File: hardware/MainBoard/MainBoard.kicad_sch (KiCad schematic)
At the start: 5 parts, among them J1 Conn_01x08_Socket, J2 Conn_01x08_Socket, J3 Conn_01x08_Socket, J4 Micro_SD_Card_Det2, U1 ESP32-S3-WROOM-1

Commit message: added more stuff to main board
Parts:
- added BZ1: Buzzer, Buzzer_Beeper:Buzzer_Mallory_AST1109MLTRQ, symbol Device:Buzzer
- added P1: USB_C_Plug_USB2.0, Connector_USB:USB_C_Receptacle_Amphenol_12401610E4-2A, symbol Connector:USB_C_Plug_USB2.0
- J4: footprint (none) -> Connector_Card:microSD_HC_Hirose_DM3AT-SF-PEJM5
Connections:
- net USB-: now reaches U1.13 (USB_D-)
- net USB-: now also P1.A7 (D-)
- net USB+: now reaches U1.14 (USB_D+)
- net USB+: now also P1.A6 (D+)
- new net: P1.A1 (GND), P1.A12 (GND), P1.B1 (GND), P1.B12 (GND)
- new net: P1.A4 (VBUS), P1.A9 (VBUS), P1.B4 (VBUS), P1.B9 (VBUS)
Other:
- moved on the sheet: J1, J3, U1

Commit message: finished usb and voltage regulator
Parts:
- removed P1: USB_C_Plug_USB2.0, Connector_USB:USB_C_Receptacle_Amphenol_12401610E4-2A, symbol Connector:USB_C_Plug_USB2.0
- added C1: 10uF, symbol Device:C
- added C2, C4: 10uF, symbol Device:C_Small
- added C3, C5: 0u1F, symbol Device:C_Small
- added D1: 1N5819WS, Diode_SMD:D_SOD-323, symbol Diode:1N5819WS
- added D2, D3, D4: D_TVS_Small_Filled, symbol Device:D_TVS_Small_Filled
- added D5: PWRLED, symbol Device:LED
- added J5: USB_C_Receptacle_USB2.0_16P, symbol Connector:USB_C_Receptacle_USB2.0_16P
- added R1, R2: 5k1, symbol Device:R
- added R3: 75, symbol Device:R_Small
- added U2: AMS1117-3.3, Package_TO_SOT_SMD:SOT-223-3_TabPin2, symbol Regulator_Linear:AMS1117-3.3
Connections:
- net GND: now also C1.2, C2.2, C3.2, C4.2, C5.2, D2.2 (A2), D3.2 (A2), D4.2 (A2), D5.1 (K), J5.A1 (GND), J5.A12 (GND), J5.B1 (GND), J5.B12 (GND), J5.S1 (SHIELD), R1.2, R2.2, U2.1 (GND)
- net USB+: now also D4.1 (A1), J5.A6 (D+), J5.B6 (D+)
- net USB-: now also D3.1 (A1), J5.A7 (D-), J5.B7 (D-)
- new net: J5.A5 (CC1), R2.1
- new net: D1.2 (A), D2.1 (A1), J5.A4 (VBUS), J5.A9 (VBUS), J5.B4 (VBUS), J5.B9 (VBUS)
- new net: J5.B5 (CC2), R1.1
- new net: D5.2 (A), R3.2
- new net VCC_3V3: C4.1, C5.1, R3.1, U2.2 (VO)
- new net VCC_5V: C1.1, C2.1, C3.1, D1.1 (K), U2.3 (VI)
- no-connect marks 0 -> 2
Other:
- note added: "USB-C"
- note added: "Voltage Regulator"
- moved on the sheet: J1, J2, J3

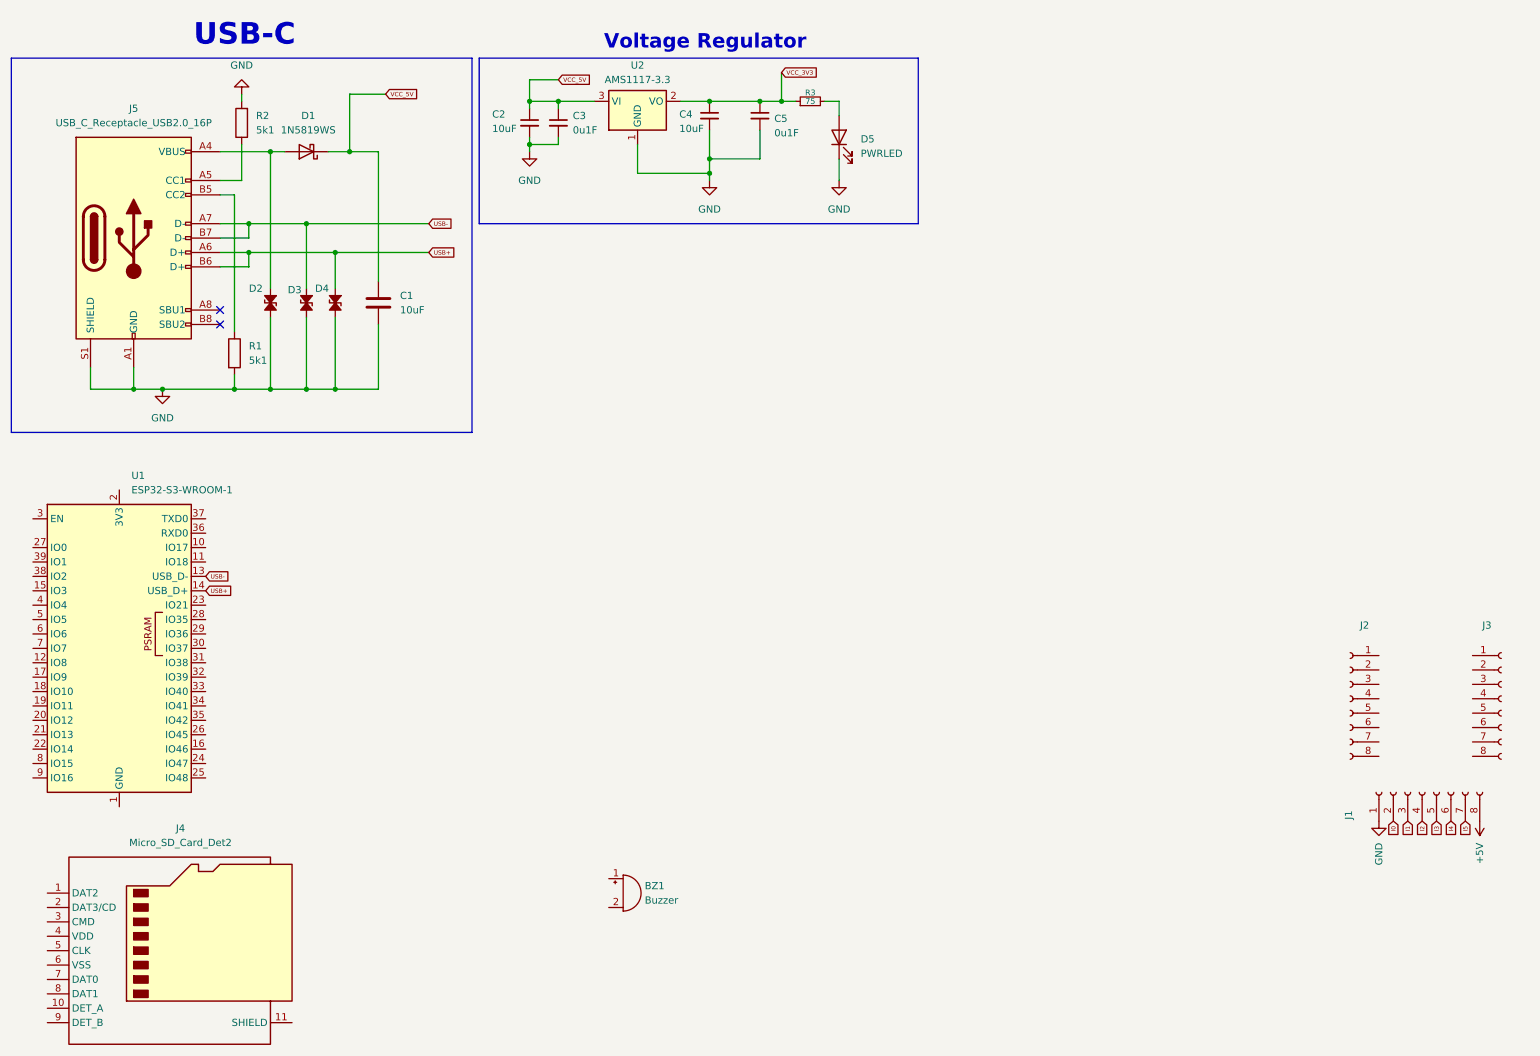
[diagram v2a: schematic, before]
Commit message: added buttons to main board
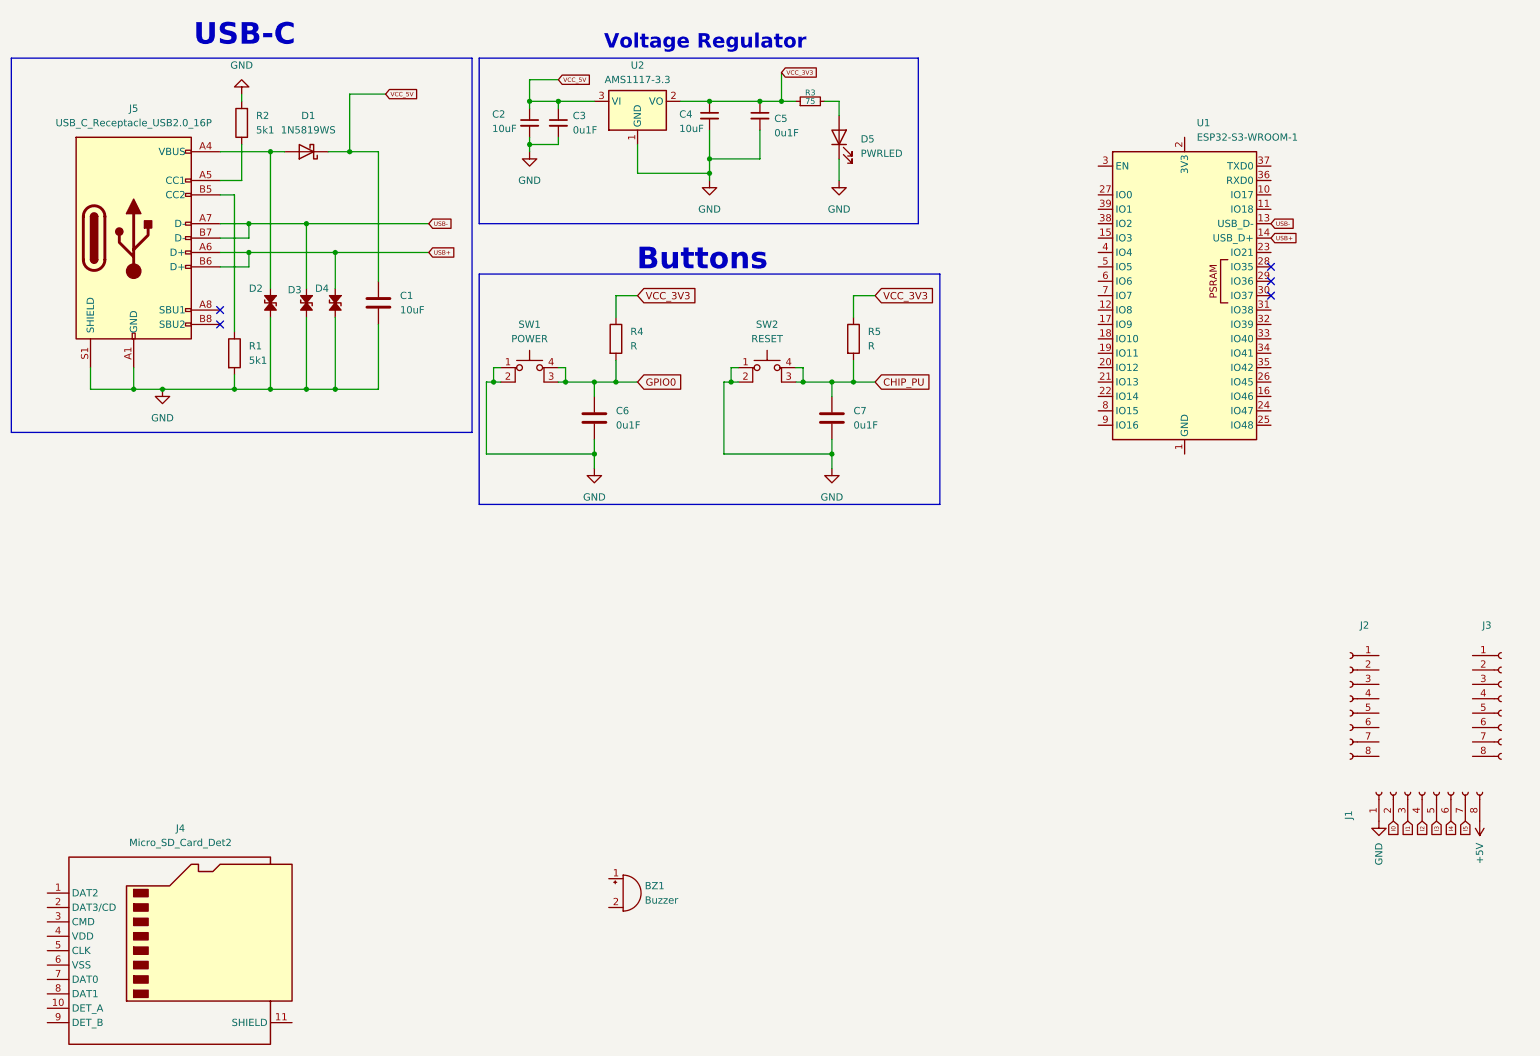
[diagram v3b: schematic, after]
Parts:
- added C6, C7: 0u1F, symbol Device:C
- added R4, R5: R, symbol Device:R
- added SW1: POWER, symbol Switch:SW_MEC_5E
- added SW2: RESET, symbol Switch:SW_MEC_5E
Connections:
- net GND: now also C6.2, C7.2, SW1.1, SW1.2, SW2.1, SW2.2
- net VCC_3V3: now also R4.1, R5.1
- new net CHIP_PU: C7.1, R5.2, SW2.3 (K), SW2.4 (A)
- new net GPIO0: C6.1, R4.2, SW1.3 (K), SW1.4 (A)
- no-connect marks 2 -> 5
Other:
- note added: "Buttons"
- moved on the sheet: U1

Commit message: added another voltage regulator
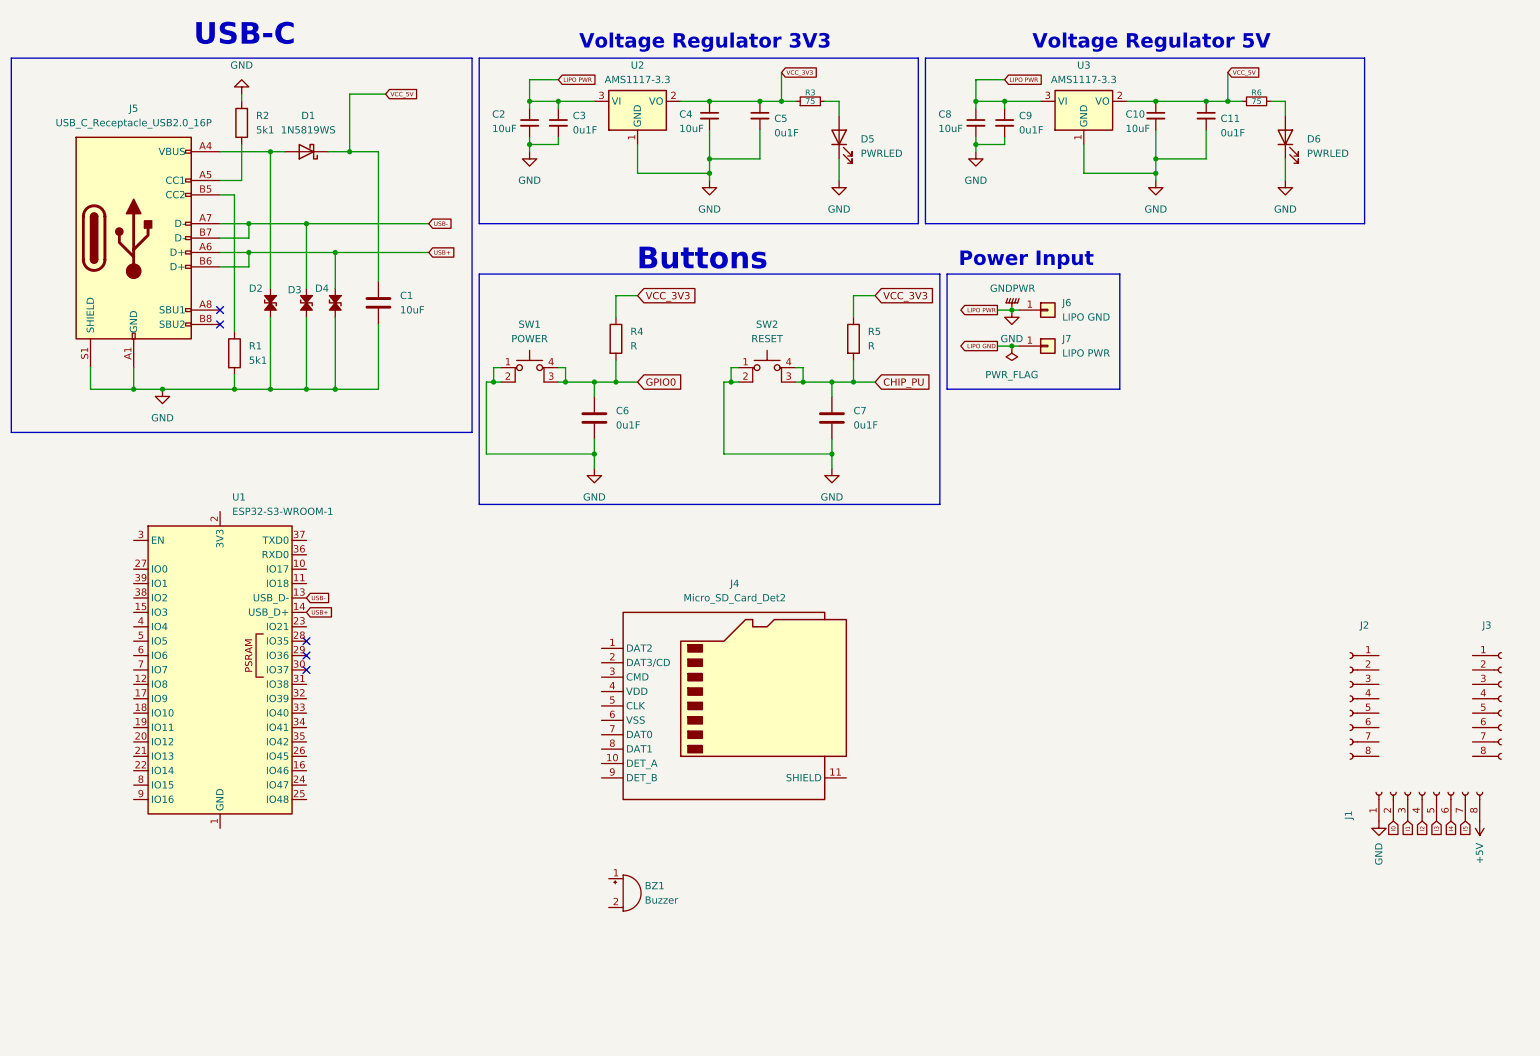
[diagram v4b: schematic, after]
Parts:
- added C10, C8: 10uF, symbol Device:C_Small
- added C11, C9: 0u1F, symbol Device:C_Small
- added D6: PWRLED, symbol Device:LED
- added J6: LIPO GND, TestPoint:TestPoint_Pad_4.0x4.0mm, symbol Connector_Generic:Conn_01x01
- added J7: LIPO PWR, TestPoint:TestPoint_Pad_4.0x4.0mm, symbol Connector_Generic:Conn_01x01
- added R6: 75, symbol Device:R_Small
- added U3: AMS1117-3.3, Package_TO_SOT_SMD:SOT-223-3_TabPin2, symbol Regulator_Linear:AMS1117-3.3
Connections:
- net GND: now also C2.1, C3.1, U2.3 (VI), C10.2, C11.2, C8.1, C8.2, C9.1, C9.2, D6.1 (K), J6.1 (Pin_1), U3.1 (GND), U3.3 (VI)
- net VCC_5V: now also C10.1, C11.1, R6.1, U3.2 (VO); no longer C2.1, C3.1, U2.3 (VI)
- new net: D6.2 (A), R6.2
- new net LIPO GND: J7.1 (Pin_1)
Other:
- note added: "Power Input"
- note added: "Voltage Regulator 3V3"
- note added: "Voltage Regulator 5V"
- note removed: "Voltage Regulator"
- moved on the sheet: J4, U1

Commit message: added lots of things to main board
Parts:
- removed D6: PWRLED, symbol Device:LED
- removed SW1: POWER, symbol Switch:SW_MEC_5E
- removed SW2: RESET, symbol Switch:SW_MEC_5E
- added BOOT1: RESET, Button_Switch_SMD:SW_Push_1P1T_NO_CK_KMR2, symbol Switch:SW_Push
- added C12, C15: 10uF, Capacitor_SMD:C_0805_2012Metric, symbol Device:C
- added C13: 100nF, Capacitor_SMD:C_0402_1005Metric, symbol Device:C
- added C14: 1uF, Capacitor_SMD:C_0603_1608Metric, symbol Device:C
- added C16: 0u1F, Capacitor_SMD:C_0402_1005Metric, symbol Device:C
- added R10, R12, R13, R8, R9: 10k, symbol Device:R_Small
- added R7: 10k, Resistor_SMD:R_1206_3216Metric, symbol Device:R
- added RESET1: BOOT, Button_Switch_SMD:SW_Push_1P1T_NO_CK_KMR2, symbol Switch:SW_Push
- C1, C10, C2, C4, C8: footprint (none) -> Capacitor_SMD:C_0805_2012Metric
- C11, C3, C5, C6, C7, C9: footprint (none) -> Capacitor_SMD:C_0402_1005Metric
- D2, D3, D4: footprint (none) -> Diode_SMD:D_0805_2012Metric
- D5: footprint (none) -> LED_SMD:LED_0603_1608Metric
- J5: footprint (none) -> Connector_USB:USB_C_Receptacle_GCT_USB4085
- R1, R2, R3, R6: footprint (none) -> Resistor_SMD:R_1206_3216Metric
- R4, R5: value R -> 10k; footprint (none) -> Resistor_SMD:R_1206_3216Metric
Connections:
- net I5 is gone; now on net SELECT RETURN: J1.7 (Pin_7)
- net VCC_3V3 is gone; now on net ESP_3V3: C4.1, C5.1, R3.1, R4.1, R5.1, U2.2 (VO)
- net CHIP_PU: now also U1.3 (EN), C14.1, R7.2, RESET1.2
- net GND: now also BZ1.2 (-), J4.11 (SHIELD), J4.6 (VSS), R6.2, U1.1 (GND), U1.40 (GND), U1.41 (GND), BOOT1.1, C12.2, C13.2, C14.2, C15.2, C16.2, RESET1.1; no longer C2.1, C3.1, C8.1, C9.1, J6.1 (Pin_1), U2.3 (VI), U3.3 (VI)
- net GPIO0: now also U1.27 (IO0), BOOT1.2
- net I0: now also U1.26 (IO45)
- net I1: now also U1.25 (IO48)
- net I2: now also U1.23 (IO21)
- net I3: now also U1.24 (IO47)
- net I4: now also U1.22 (IO14)
- net SD_DAT2: now reaches J4.1 (DAT2)
- net SD_DAT2: now also U1.34 (IO41), R8.2
- net SD_DET: now reaches J4.10 (DET_A)
- net SD_DET: now also J4.9 (DET_B), U1.31 (IO38)
- net SD_DAT3: now reaches J4.2 (DAT3/CD)
- net SD_DAT3: now also U1.33 (IO40), R9.2
- net SD_CMD: now reaches J4.3 (CMD)
- net SD_CMD: now also U1.32 (IO39), R10.2
- net ESP_3V3: now reaches J4.4 (VDD)
- net ESP_3V3: now also U1.2 (3V3), C12.1, C13.1, C15.1, C16.1, R10.1, R12.1, R13.1, R7.1, R8.1, R9.1
- net SD_CLK: now reaches J4.5 (CLK)
- net SD_CLK: now also U1.30 (IO37)
- net SD_DAT0: now reaches J4.7 (DAT0)
- net SD_DAT0: now also U1.29 (IO36), R12.2
- net SD_DAT1: now reaches J4.8 (DAT1)
- net SD_DAT1: now also U1.28 (IO35), R13.2
- net BZR: now reaches BZ1.1 (+)
- net SELECT RETURN: now reaches U1.21 (IO13)
- net LIPO GND renamed GNDPWR
- new net LIPO PWR: C2.1, C3.1, C8.1, C9.1, J6.1 (Pin_1), U2.3 (VI), U3.3 (VI)
- no-connect marks 5 -> 2
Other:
- note added: "Buzzer"
- note added: "ESP32-S3-WROOM-1"
- note added: "SD Card"
- moved on the sheet: BZ1, J1, J2, J3, J4, J6, J7, U1

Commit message: more main board stuff
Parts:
- BZ1: footprint Buzzer_Beeper:Buzzer_Mallory_AST1109MLTRQ -> Buzzer_Beeper:MagneticBuzzer_Kingstate_KCG0601
- R10, R12, R13, R8, R9: footprint (none) -> Resistor_SMD:R_1206_3216Metric
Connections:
- net DATA8: now reaches J2.1 (Pin_1)
- net DATA8: now also U1.7 (IO7)
- net DATA9: now reaches J2.2 (Pin_2)
- net DATA9: now also U1.8 (IO15)
- net DATA10: now reaches J2.3 (Pin_3)
- net DATA10: now also U1.9 (IO16)
- net DATA11: now reaches J2.4 (Pin_4)
- net DATA11: now also U1.10 (IO17)
- net DATA12: now reaches J2.5 (Pin_5)
- net DATA12: now also U1.11 (IO18)
- net DATA13: now reaches J2.6 (Pin_6)
- net DATA13: now also U1.12 (IO8)
- net DATA14: now reaches J2.7 (Pin_7)
- net DATA14: now also U1.15 (IO3)
- net DATA15: now reaches J2.8 (Pin_8)
- net DATA15: now also U1.16 (IO46)
- net DATA7: now reaches J3.1 (Pin_1)
- net DATA7: now also U1.35 (IO42)
- net DATA6: now reaches J3.2 (Pin_2)
- net DATA6: now also U1.36 (RXD0)
- net DATA5: now reaches J3.3 (Pin_3)
- net DATA5: now also U1.37 (TXD0)
- net DATA4: now reaches J3.4 (Pin_4)
- net DATA4: now also U1.38 (IO2)
- net DATA3: now reaches J3.5 (Pin_5)
- net DATA3: now also U1.39 (IO1)
- net DATA2: now reaches J3.6 (Pin_6)
- net DATA2: now also U1.6 (IO6)
- net DATA1: now reaches J3.7 (Pin_7)
- net DATA1: now also U1.5 (IO5)
- net DATA0: now reaches J3.8 (Pin_8)
- net DATA0: now also U1.4 (IO4)
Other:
- note added: "Hat Connection Interface"
- note added: "LiPo Power Input"
- note removed: "Power Input"
- moved on the sheet: BZ1, J1, J2, J3, J6, J7

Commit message: finished main board
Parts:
- removed RESET1: BOOT, Button_Switch_SMD:SW_Push_1P1T_NO_CK_KMR2, symbol Switch:SW_Push
- removed U3: AMS1117-3.3, Package_TO_SOT_SMD:SOT-223-3_TabPin2, symbol Regulator_Linear:AMS1117-3.3
- added D6: PWRLED, LED_SMD:LED_0603_1608Metric, symbol Device:LED
- added J8: En_A, TestPoint:TestPoint_Pad_1.5x1.5mm, symbol Connector_Generic:Conn_01x01
- added J9: En_B, TestPoint:TestPoint_Pad_1.5x1.5mm, symbol Connector_Generic:Conn_01x01
- added Q1: MMBT2222A, Package_TO_SOT_SMD:SOT-23W_Handsoldering, symbol Transistor_BJT:MMBT2222A
- added U3: AMS1117-5.0, Package_TO_SOT_SMD:SOT-223-3_TabPin2, symbol Regulator_Linear:AMS1117-5.0
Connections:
- net GNDPWR is gone; now on net GND: J7.1 (Pin_1)
- net BZR: now also U1.18 (IO10)
- net CHIP_PU: now also J9.1 (Pin_1); no longer R5.2
- net GND: now also D6.1 (K), U3.1 (GND); no longer R6.2
- net I2: now also U1.24 (IO47); no longer U1.23 (IO21)
- net I3: now also U1.23 (IO21); no longer U1.24 (IO47)
- net LIPO PWR: now also U3.3 (VI)
- net SD_CLK: now also U1.32 (IO39); no longer U1.30 (IO37)
- net SD_CMD: now also U1.30 (IO37); no longer U1.32 (IO39)
- net SD_DAT0: now also U1.33 (IO40); no longer U1.29 (IO36)
- net SD_DAT1: now also U1.34 (IO41); no longer U1.28 (IO35)
- net SD_DAT2: now also U1.28 (IO35); no longer U1.34 (IO41)
- net SD_DAT3: now also U1.29 (IO36); no longer U1.33 (IO40)
- net VCC_5V: now also Q1.3 (C), U3.2 (VO)
- net HATS_ENABLE: now reaches U1.20 (IO12)
- net HATS_ENABLE: now also Q1.1 (B)
- net +5V: no longer names the net of J1.8 (Pin_8)
- net +5V: now also Q1.2 (E)
- new net: J8.1 (Pin_1), R5.2
- new net: D6.2 (A), R6.2
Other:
- moved on the sheet: C7, J1, R5
